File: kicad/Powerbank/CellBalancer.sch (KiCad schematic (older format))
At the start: 45 parts, among them IC1 BQ4050RSMR, IC2 SN74LVC1G14DSFR, IC3 SN74LVC1G08DSFR, Q1 Q_NMOS_GDS, Q2 Q_PMOS_GDS, Q3 Q_NMOS_GDS

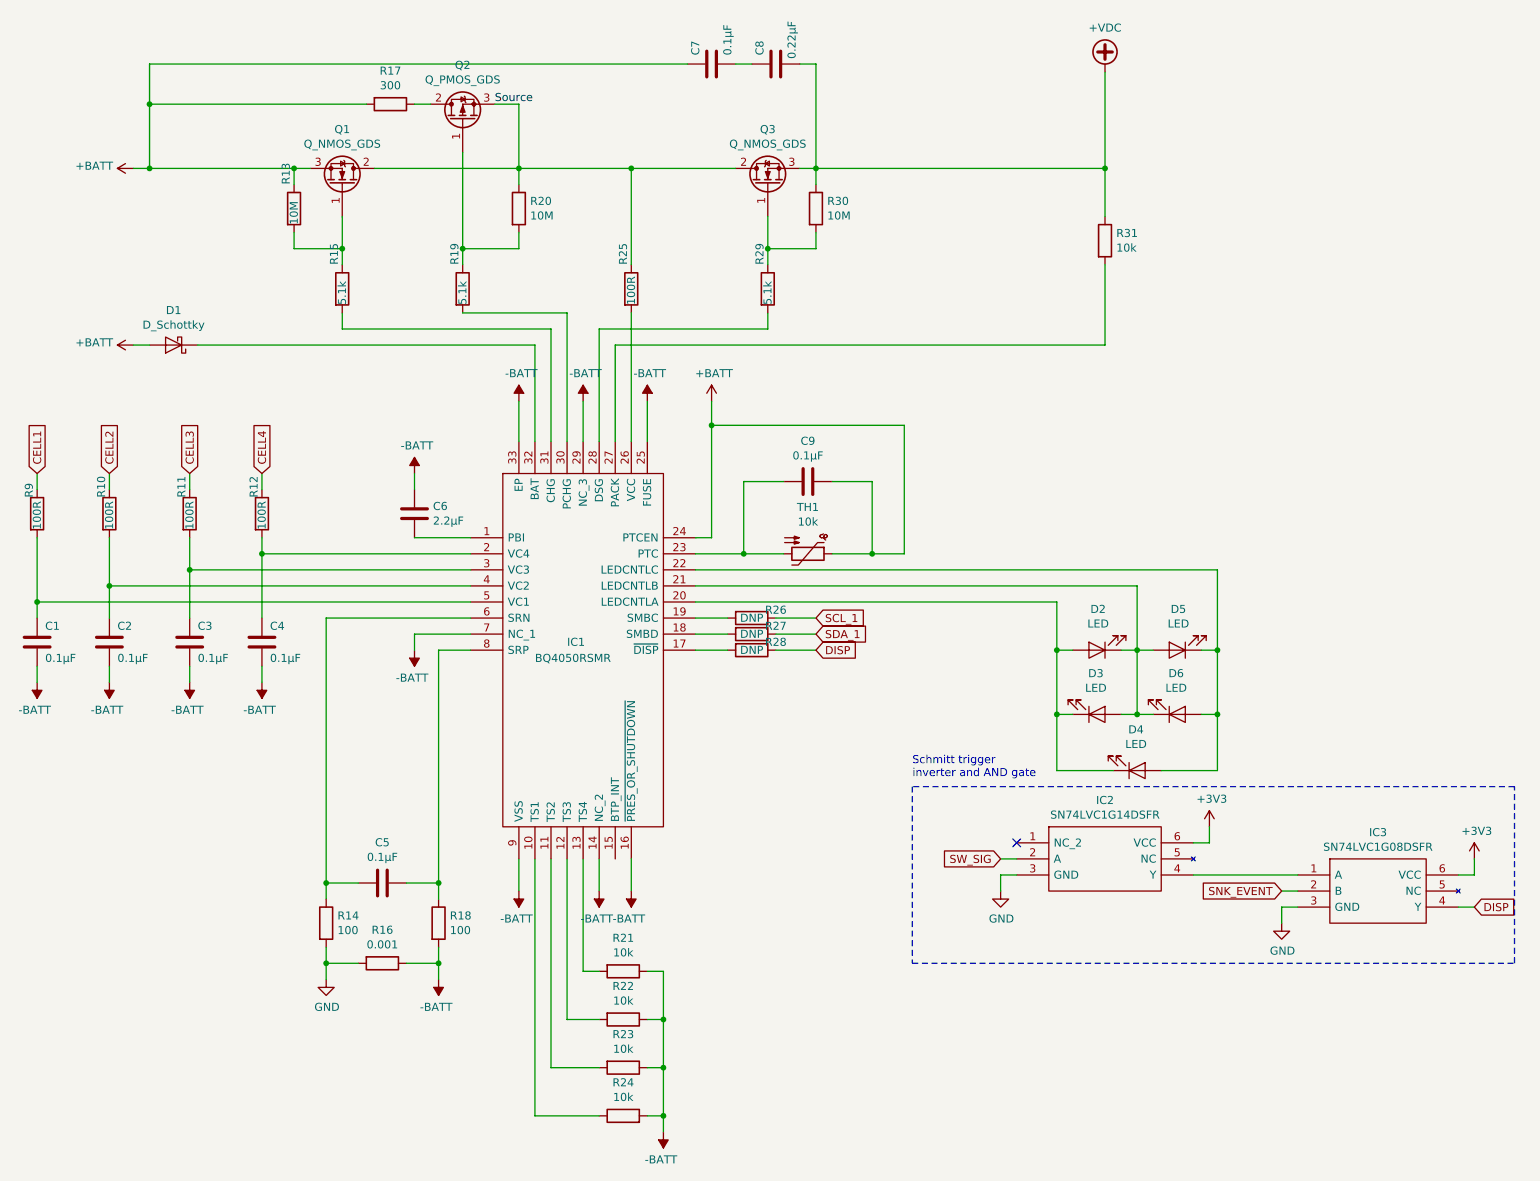
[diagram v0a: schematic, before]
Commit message: Updated layout in schematic for nicer look
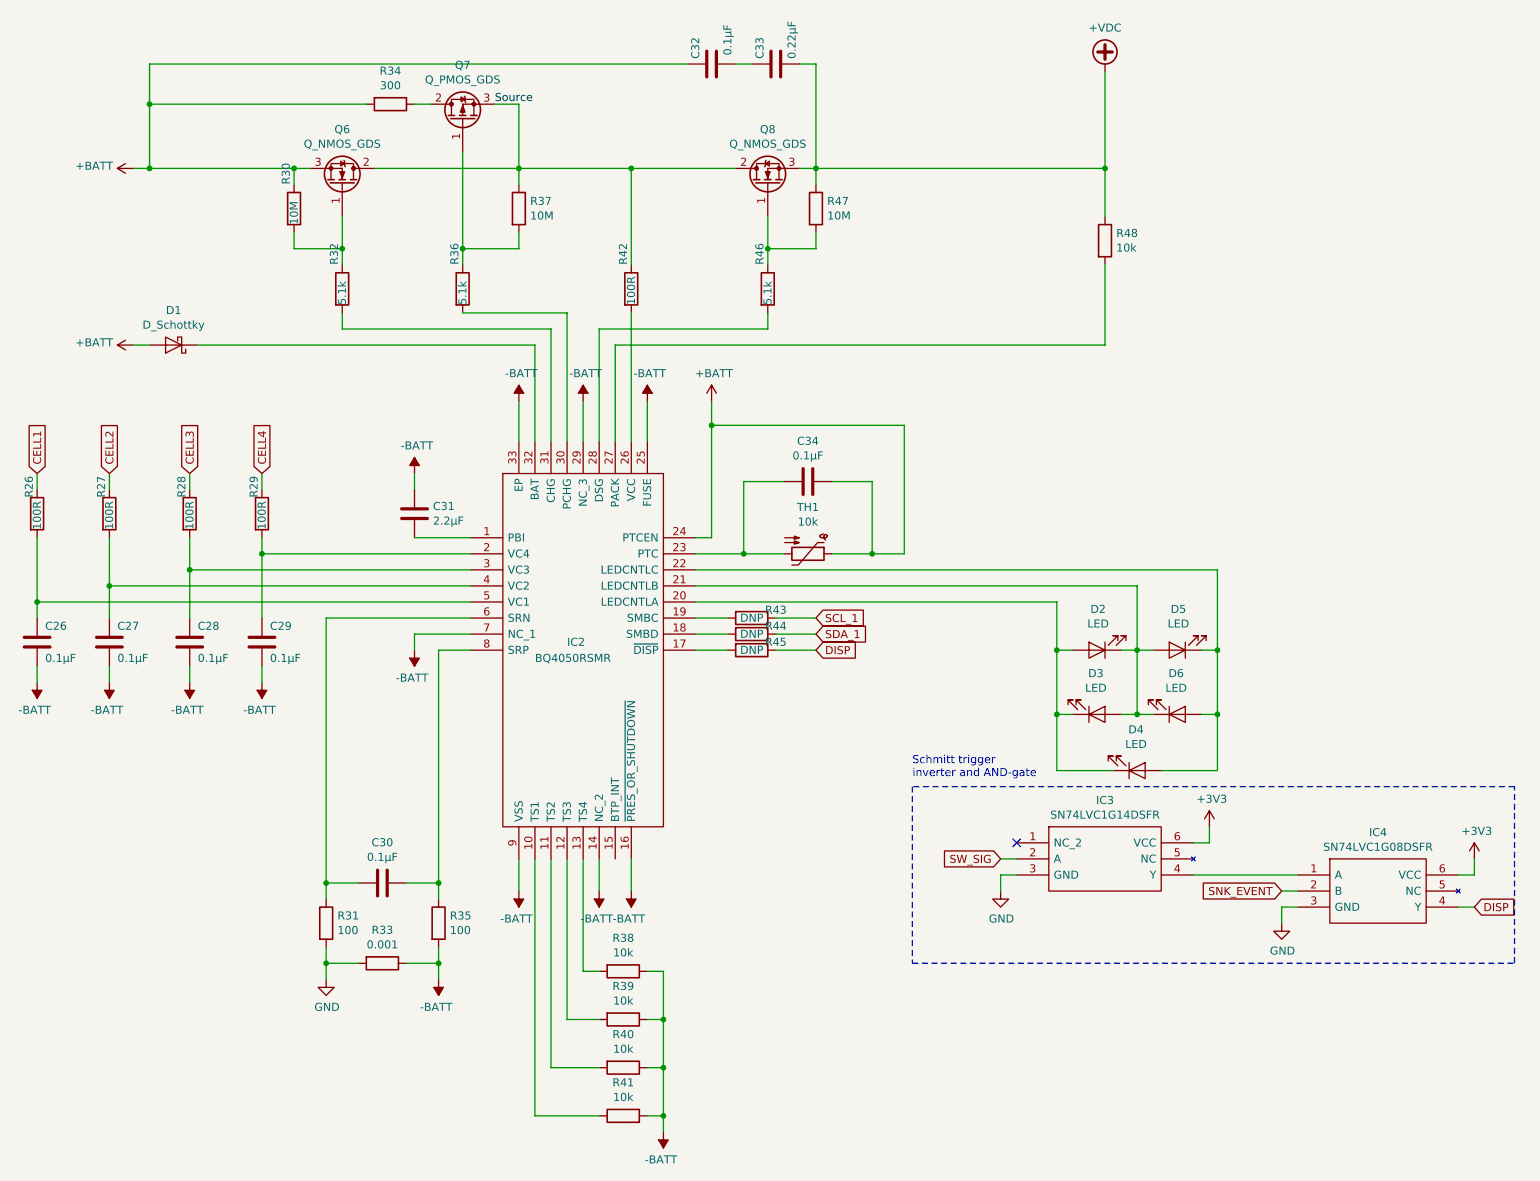
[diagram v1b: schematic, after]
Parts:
- renumbered C1 to C26, C2 to C27, C3 to C28, C4 to C29, C5 to C30, C6 to C31, C7 to C32, C8 to C33, C9 to C34, IC1 to IC2, IC2 to IC3, IC3 to IC4, Q1 to Q6, Q2 to Q7, Q3 to Q8, R9 to R26, R10 to R27, R11 to R28, R12 to R29, R13 to R30, R14 to R31, R15 to R32, R16 to R33, R17 to R34, R18 to R35, R19 to R36, R20 to R37, R21 to R38, R22 to R39, R23 to R40, R24 to R41, R25 to R42, R26 to R43, R27 to R44, R28 to R45, R29 to R46, R30 to R47, R31 to R48
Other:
- note added: "Schmitt trigger \ninverter and AND-gate"
- note removed: "Schmitt trigger \ninverter and AND gate"
